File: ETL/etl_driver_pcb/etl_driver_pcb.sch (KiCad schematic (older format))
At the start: 10 parts, among them J1 from Arduino, J2 12V power, J3 to_ETL, Q1 BD441, U1 CA3140

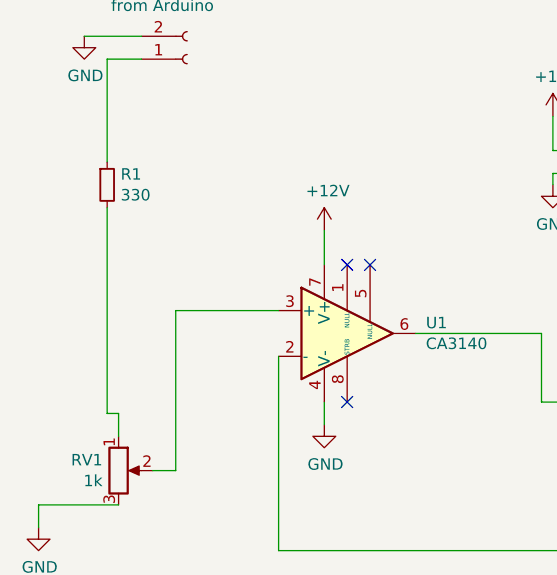
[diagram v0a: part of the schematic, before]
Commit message: add arduino due shield for lens driver
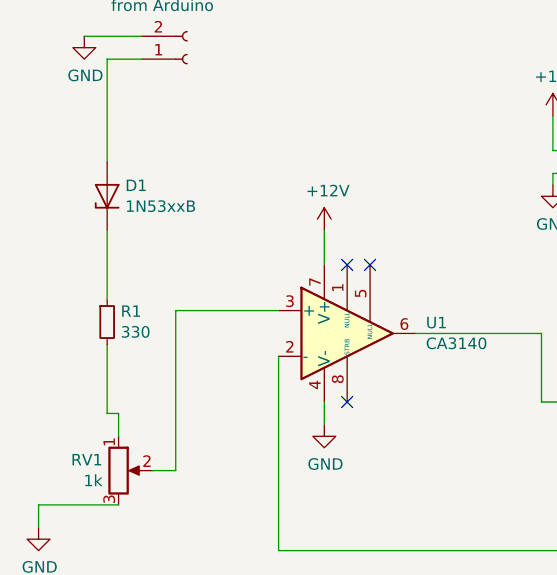
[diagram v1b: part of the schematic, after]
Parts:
- added D1: 1N53xxB, Diode_THT:D_DO-201_P15.24mm_Horizontal, symbol Diode:1N53xxB
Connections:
- net at R1.1: now also D1.1 (K); no longer J1.1 (Pin_1)
- new net: D1.2 (A), J1.1 (Pin_1)
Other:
- moved on the sheet: R1
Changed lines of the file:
@@
 L Device:R_Small R1
 U 1 1 5E591D42
-P 4150 3100
-F 0 "R1" H 4209 3146 50  0000 L CNN
-F 1 "330" H 4209 3055 50  0000 L CNN
-F 2 "Resistor_THT:R_Axial_DIN0207_L6.3mm_D2.5mm_P10.16mm_Horizontal" H 4150 3100 50  0001 C CNN
-F 3 "~" H 4150 3100 50  0001 C CNN
-	1    4150 3100
+P 4150 3700
+F 0 "R1" H 4209 3746 50  0000 L CNN
+F 1 "330" H 4209 3655 50  0000 L CNN
+F 2 "Resistor_THT:R_Axial_DIN0207_L6.3mm_D2.5mm_P10.16mm_Horizontal" H 4150 3700 50  0001 C CNN
+F 3 "~" H 4150 3700 50  0001 C CNN
+	1    4150 3700
 	1    0    0    -1
 $EndComp
@@
 	4150 2550 4300 2550
 Wire Wire Line
-	4150 3200 4150 4100
-Wire Wire Line
 	4150 4100 4200 4100
 Wire Wire Line
@@
 Wire Wire Line
 	5100 4050 5100 4150
+Wire Wire Line
+	4150 3800 4150 4100
+$Comp
+L Diode:1N53xxB D1
+U 1 1 5EA995FC
+P 4150 3150
+F 0 "D1" V 4196 3071 50  0000 R CNN
+F 1 "1N53xxB" V 4105 3071 50  0000 R CNN
+F 2 "Diode_THT:D_DO-201_P15.24mm_Horizontal" H 4150 2975 50  0001 C CNN
+F 3 "https://diotec.com/tl_files/diotec/files/pdf/datasheets/1n5345b.pdf" H 4150 3150 50  0001 C CNN
+	1    4150 3150
+	0    -1   -1   0
+$EndComp
+Wire Wire Line
+	4150 3300 4150 3600
 $EndSCHEMATC
